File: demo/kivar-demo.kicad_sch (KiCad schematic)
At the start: 0 parts

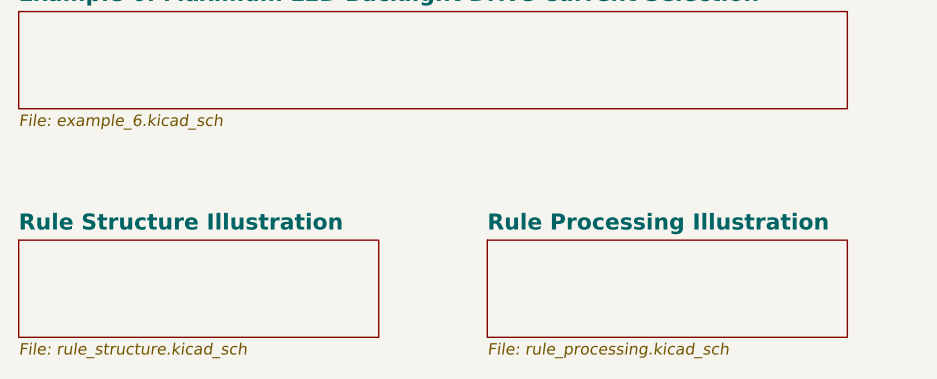
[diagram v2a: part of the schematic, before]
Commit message: Remove outdated rule structure figure, update compiler figure
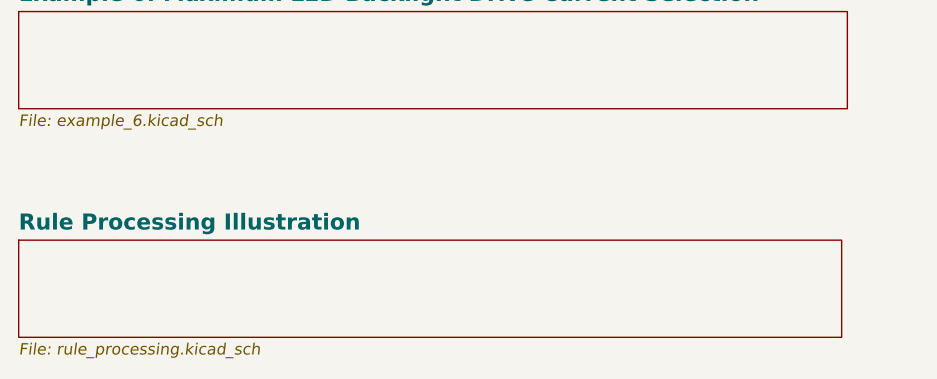
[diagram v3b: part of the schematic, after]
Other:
- removed sheet Rule Structure Illustration
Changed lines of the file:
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@@
 	)
 	(sheet
-		(at 80.01 146.05)
-		(size 40.005 10.795)
+		(at 27.94 146.05)
+		(size 91.44 10.795)
 		(fields_autoplaced yes)
 		(stroke
@@
 		)
 		(property "Sheetname" "Rule Processing Illustration"
-			(at 80.01 145.0844 0)
+			(at 27.94 145.0844 0)
 			(effects
 				(font
@@
 		)
 		(property "Sheetfile" "rule_processing.kicad_sch"
-			(at 80.01 157.4296 0)
+			(at 27.94 157.4296 0)
 			(effects
 				(font
@@
 			(project "kivar-demo"
 				(path "/cd745a5c-45fb-4106-85c8-c86c130b6ee7"
-					(page "9")
+					(page "8")
 				)
 			)
@@
 				)
 			)
-		)
-	)
-	(sheet
-		(at 27.94 146.05)
-		(size 40.005 10.795)
-		(fields_autoplaced yes)
-		(stroke
-			(width 0.1524)
-			(type solid)
-			(color 151 166 142 1)
-		)
-		(fill
-			(color 208 229 196 1.0000)
-		)
-		(property "Sheetname" "Rule Structure Illustration"
-			(at 27.94 145.0844 0)
-			(effects
-				(font
-					(size 1.778 1.778)
-					(bold yes)
-					(color 146 108 108 1)
-				)
-				(justify left bottom)
-			)
-		)
-		(property "Sheetfile" "rule_structure.kicad_sch"
-			(at 27.94 157.4296 0)
-			(effects
-				(font
-					(size 1.27 1.27)
-					(italic yes)
-					(color 194 194 194 1)
-				)
-				(justify left top)
-			)
-		)
-		(instances
-			(project "kivar-demo"
-				(path "/cd745a5c-45fb-4106-85c8-c86c130b6ee7"
-					(page "8")
-				)
-			)
